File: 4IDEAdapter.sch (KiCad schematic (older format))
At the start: 9 parts

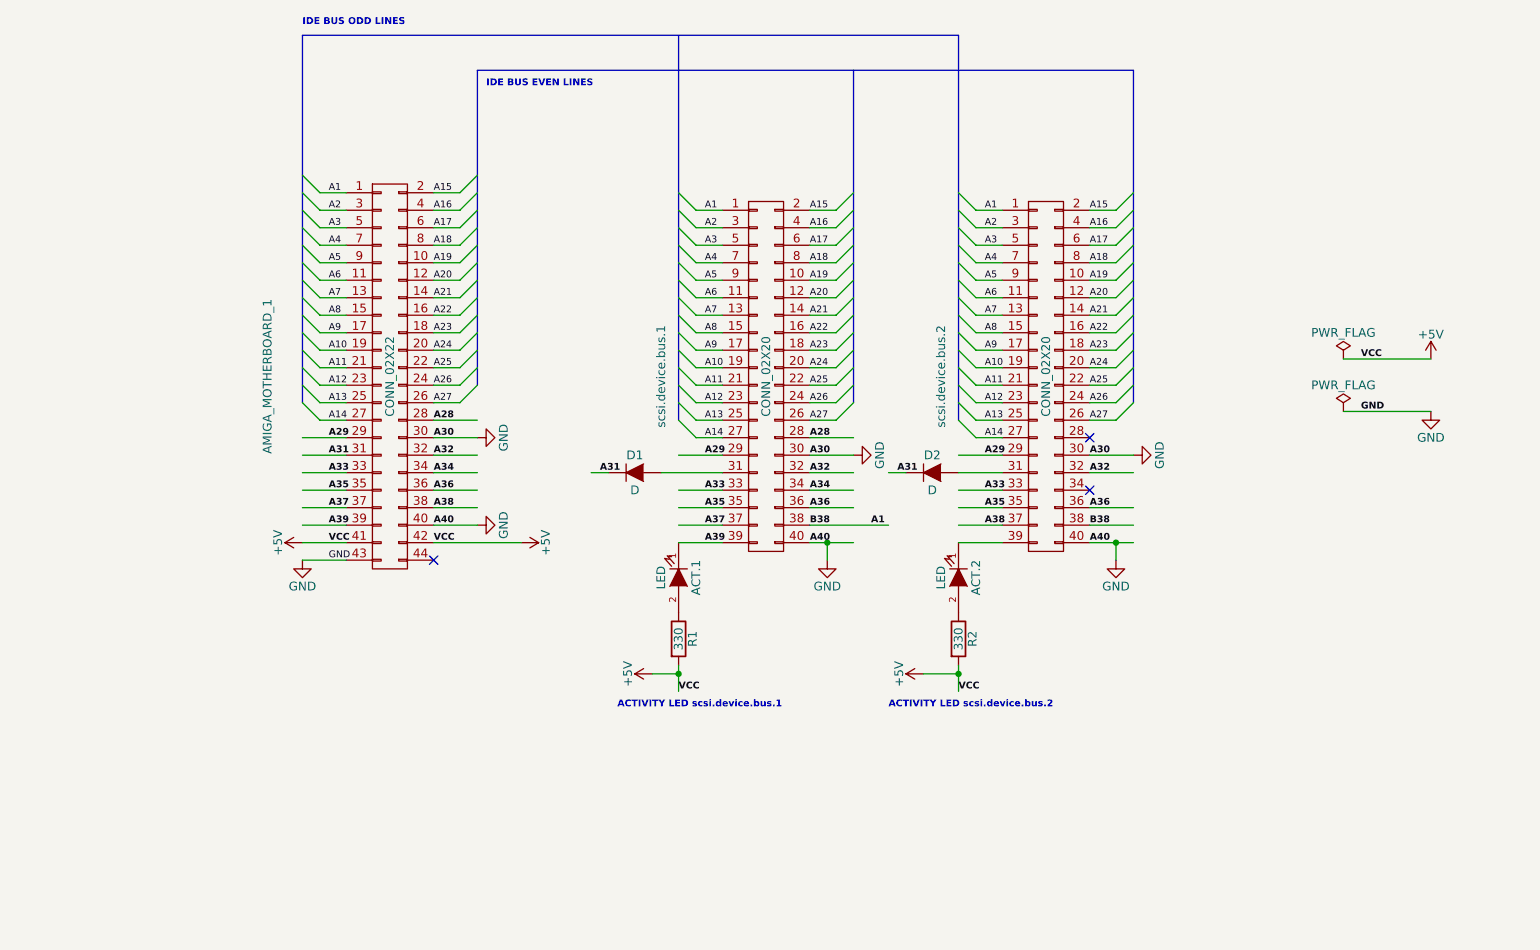
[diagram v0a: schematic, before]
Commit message: added a second ide port 44 pin
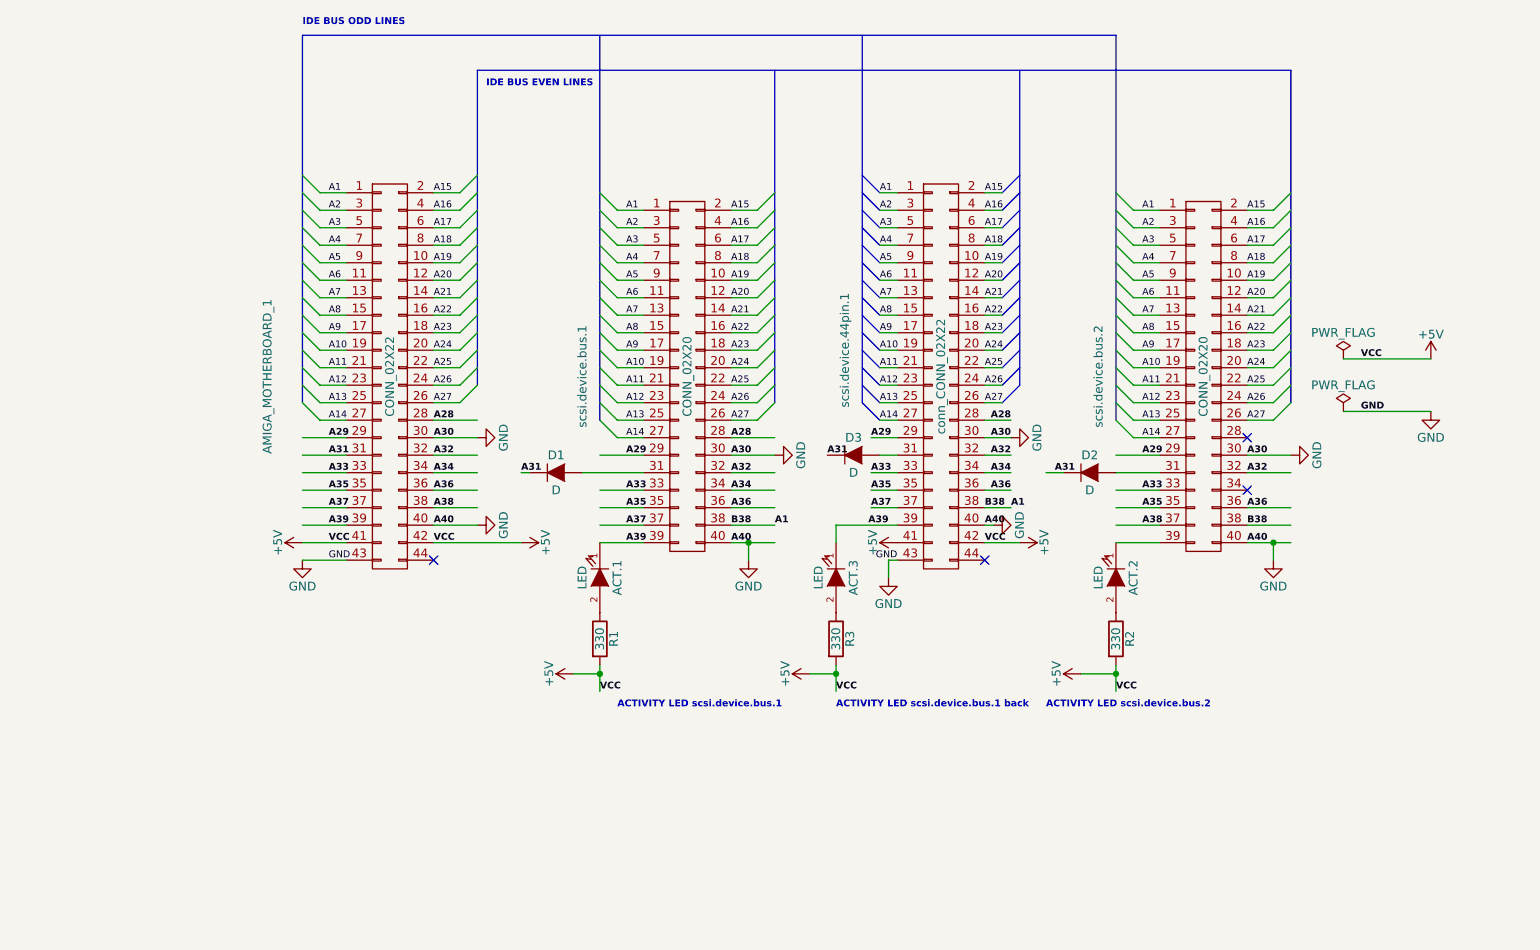
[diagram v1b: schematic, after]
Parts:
- added ACT.3: LED, LEDs:LED_1206, symbol LED
- added D3: D, Diodes_SMD:SMA_Handsoldering, symbol D
- added R3: 330, Resistors_SMD:R_1210_HandSoldering, symbol R
- added scsi.device.44pin.1: conn_CONN_02X22, RetroBitLab:PinHeader_2x22_P1.27mm_Vertical, symbol conn_CONN_02X22
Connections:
- wire segments 131 -> 177
- no-connect marks 3 -> 4
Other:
- note added: "ACTIVITY LED scsi.device.bus.1 back"
- moved on the sheet: ACT.1, ACT.2, D1, D2, R1, R2, scsi.device.bus.1, scsi.device.bus.2

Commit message: Updated connectors
The IDE44 pin connector was wrong. Due to the complexity of having 3
connectors on board the size of the board need to be increased. Now it
is almost like a Credit Card Size. It needs an Amiga 1200 or Amiga 600
placed into a TowerCase and *NOT TOO NEAR* to the bottom of the case...
But if you need a 4 devices connected, for sure the default case has not
accomplishes that!
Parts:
- AMIGA_MOTHERBOARD_1: footprint RetroBitLab:Vertical_IDE_44_Pins_2x22_1.27_PCB -> RetroBitLab:Socket_IDC_2x22_2.00mm_PCB
- R1, R2, R3: footprint Resistors_SMD:R_1210_HandSoldering -> Resistors_SMD:R_1206_HandSoldering
- scsi.device.44pin.1: footprint RetroBitLab:PinHeader_2x22_P1.27mm_Vertical -> RetroBitLab:PinHeader_2x22_P2.00mm_Vertical
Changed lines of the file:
@@
 F 0 "AMIGA_MOTHERBOARD_1" V 2600 3950 50  0000 C CNN
 F 1 "CONN_02X22" V 3300 3950 50  0000 C CNN
-F 2 "RetroBitLab:Vertical_IDE_44_Pins_2x22_1.27_PCB" H 3300 3050 50  0001 C CNN
+F 2 "RetroBitLab:Socket_IDC_2x22_2.00mm_PCB" H 3300 3050 50  0001 C CNN
 F 3 "" H 3300 3050 50  0000 C CNN
 	1    3300 3950
@@
 F 0 "R1" V 4580 5450 50  0000 C CNN
 F 1 "330" V 4500 5450 50  0000 C CNN
-F 2 "Resistors_SMD:R_1210_HandSoldering" V 4430 5450 50  0001 C CNN
+F 2 "Resistors_SMD:R_1206_HandSoldering" V 4430 5450 50  0001 C CNN
 F 3 "" H 4500 5450 50  0000 C CNN
 	1    4500 5450
@@
 F 0 "R2" V 7530 5450 50  0000 C CNN
 F 1 "330" V 7450 5450 50  0000 C CNN
-F 2 "Resistors_SMD:R_1210_HandSoldering" V 7380 5450 50  0001 C CNN
+F 2 "Resistors_SMD:R_1206_HandSoldering" V 7380 5450 50  0001 C CNN
 F 3 "" H 7450 5450 50  0000 C CNN
 	1    7450 5450
@@
 F 0 "scsi.device.44pin.1" V 5900 4100 50  0000 C CNN
 F 1 "conn_CONN_02X22" V 6450 3950 50  0000 C CNN
-F 2 "RetroBitLab:PinHeader_2x22_P1.27mm_Vertical" V 7000 4300 50  0001 C CNN
+F 2 "RetroBitLab:PinHeader_2x22_P2.00mm_Vertical" V 7000 4300 50  0001 C CNN
 F 3 "" H 6450 3050 50  0000 C CNN
 	1    6450 3950
@@
 F 0 "R3" V 5930 5450 50  0000 C CNN
 F 1 "330" V 5850 5450 50  0000 C CNN
-F 2 "Resistors_SMD:R_1210_HandSoldering" V 5780 5450 50  0001 C CNN
+F 2 "Resistors_SMD:R_1206_HandSoldering" V 5780 5450 50  0001 C CNN
 F 3 "" H 5850 5450 50  0000 C CNN
 	1    5850 5450

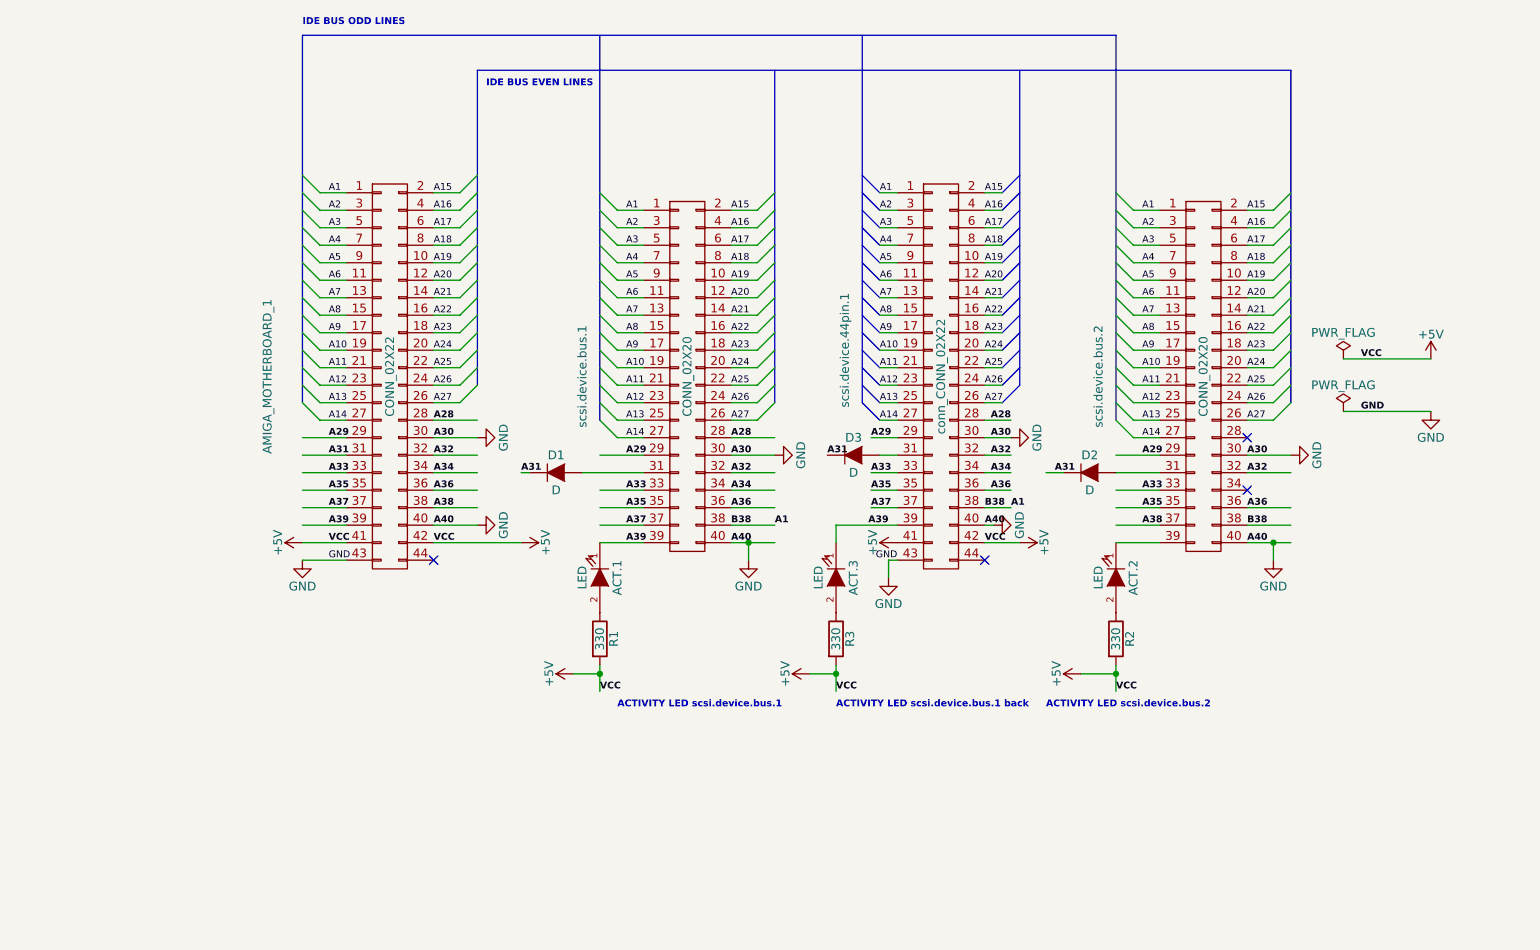
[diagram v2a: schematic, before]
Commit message: added activity led management
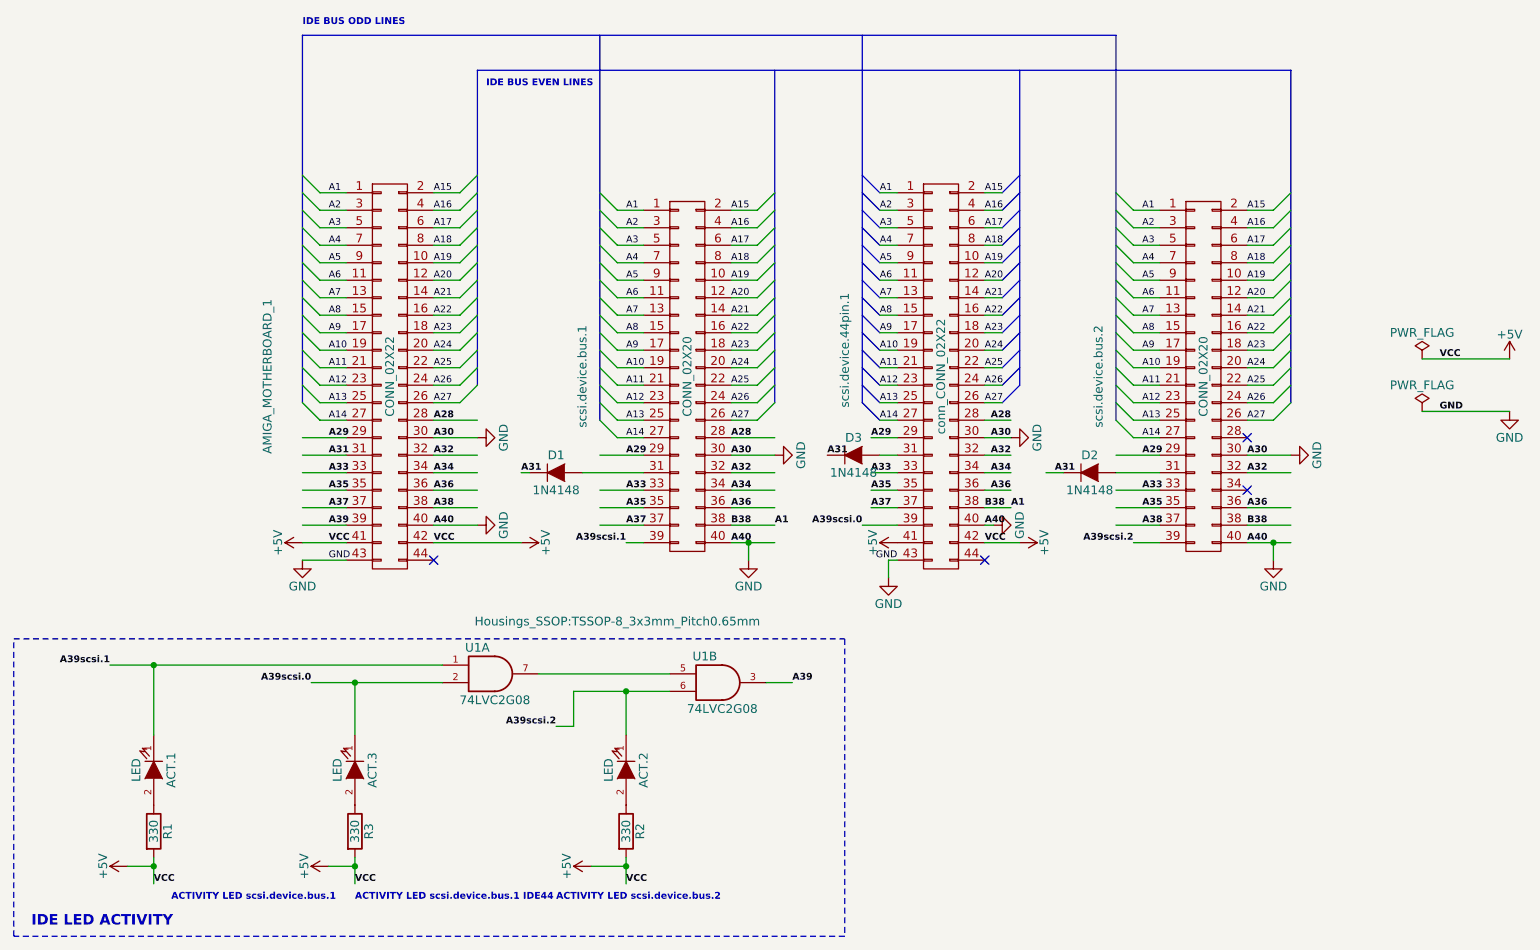
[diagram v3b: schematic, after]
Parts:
- added U1: 74LVC2G08, Housings_SSOP:TSSOP-8_3x3mm_Pitch0.65mm, symbol 74LVC2G08
- D1, D2, D3: value D -> 1N4148
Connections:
- net labels added: A39scsi.0, A39scsi.1, A39scsi.2
- wire segments 177 -> 186
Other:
- note added: "ACTIVITY LED scsi.device.bus.1 IDE44"
- note added: "IDE LED ACTIVITY"
- note removed: "ACTIVITY LED scsi.device.bus.1 back"
- moved on the sheet: ACT.1, ACT.2, ACT.3, R1, R2, R3
